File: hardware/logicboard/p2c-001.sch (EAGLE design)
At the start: 40 parts, among them IC1 74LS07N, K1 G5V1, T1 2SC1815

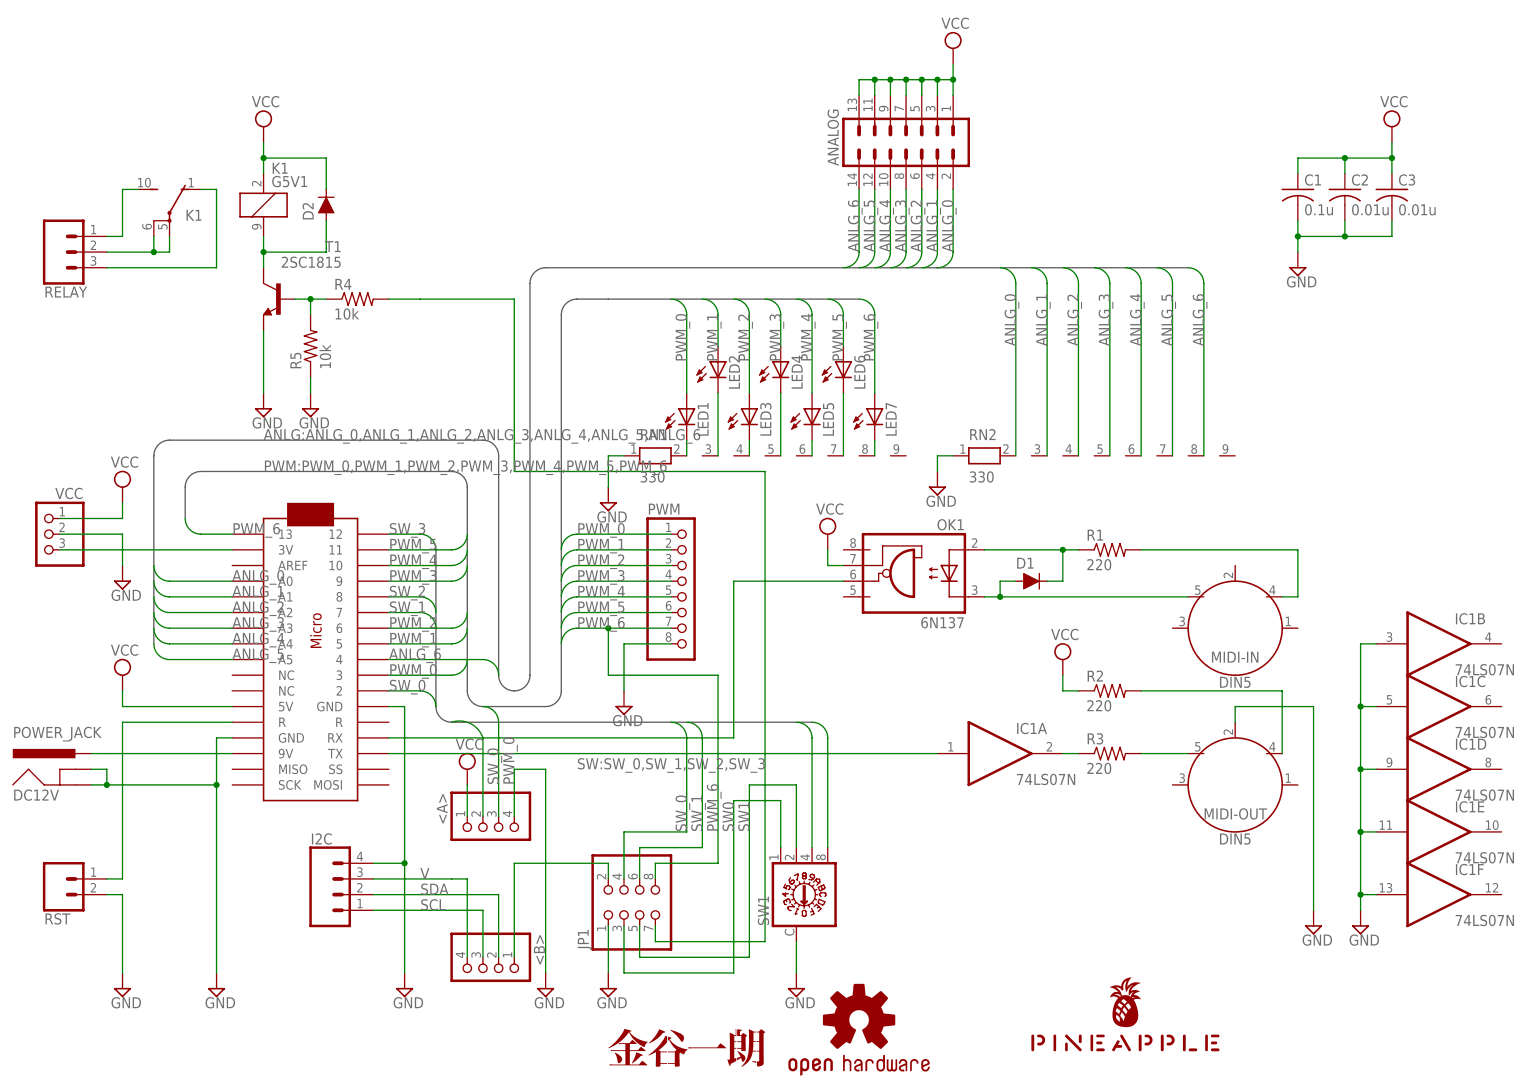
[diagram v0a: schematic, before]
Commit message: Alternative DC and MIDI connectors.
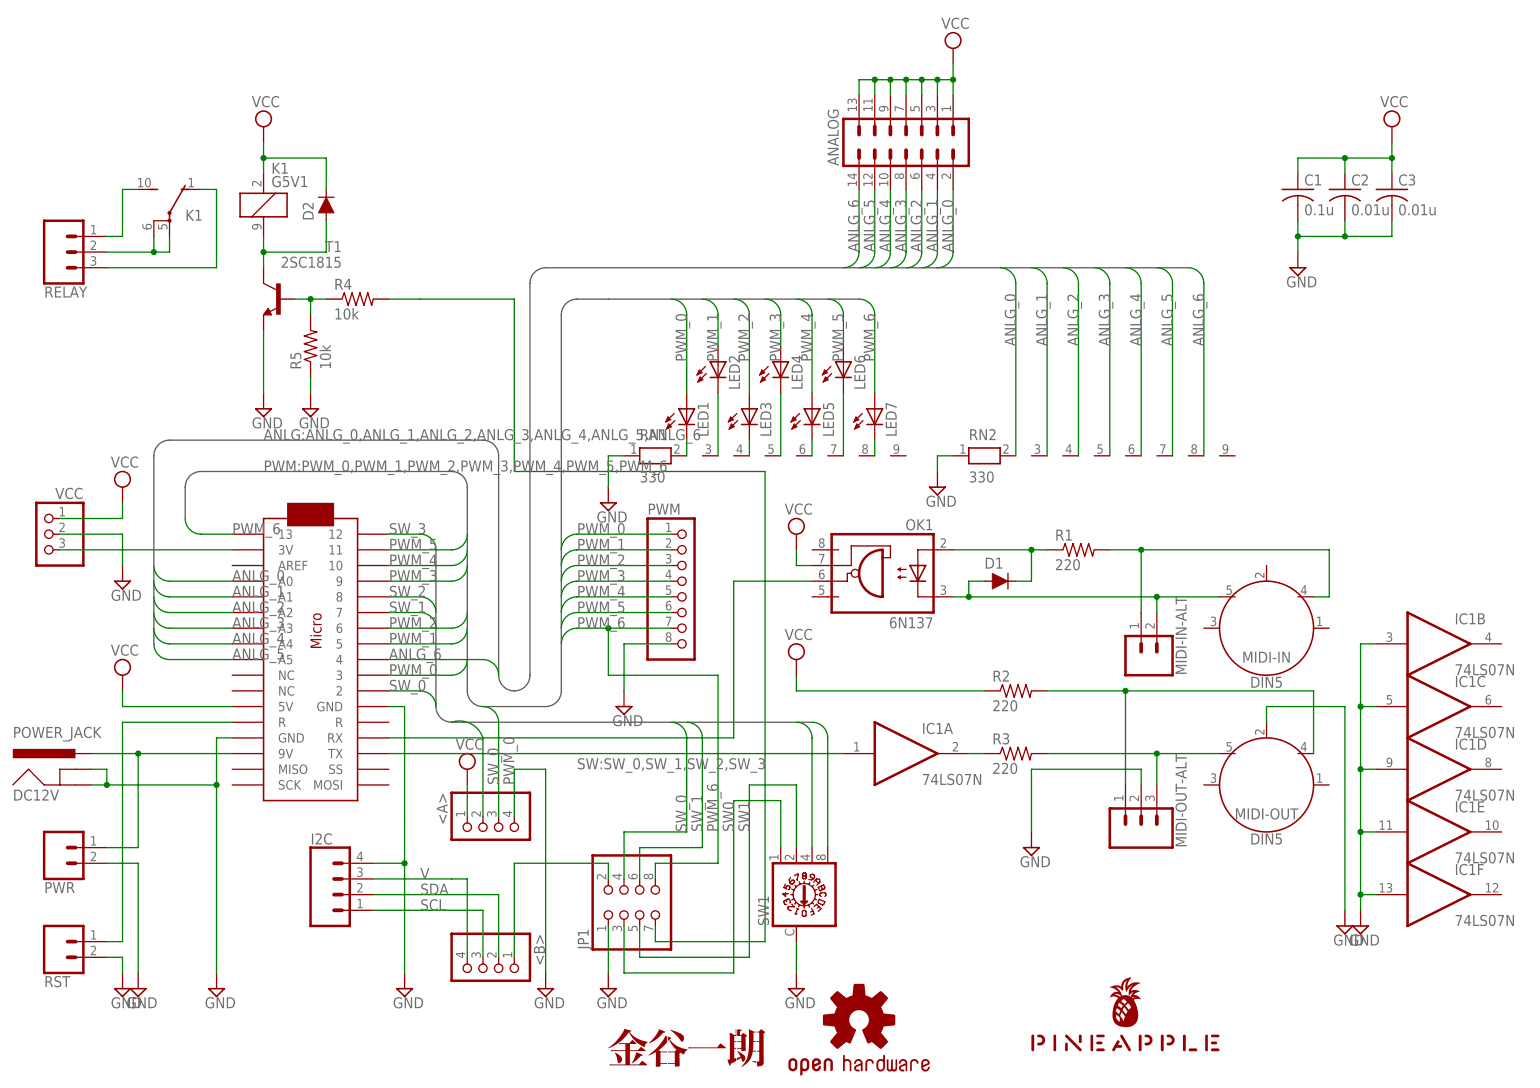
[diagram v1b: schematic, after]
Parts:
- added MIDI-IN-ALT: (no value), SparkFun-Connectors:CONN_02JST-PTH-2
- added MIDI-OUT-ALT: (no value), SparkFun-Connectors:CONN_03JST-PTH
- added PWR: (no value), SparkFun-Connectors:CONN_02
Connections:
- net GND: now also MIDI-OUT-ALT.2, PWR.2
- net MIDIIN+: now also MIDI-IN-ALT.1
- net MIDIIN-: now also MIDI-IN-ALT.2
- net MIDIOUT+: now also MIDI-OUT-ALT.1
- net MIDIOUT-: now also MIDI-OUT-ALT.3
- net VIN: now also PWR.1
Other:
- moved on the sheet: D1, IC1A, MIDI-IN, MIDI-OUT, OK1, R1, R2, R3, RST

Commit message: QR Code.
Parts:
- added U$4: CARD_QR, pineapple_card_qr:CARD_QR
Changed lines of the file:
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@@
 <part name="PWR" library="SparkFun-Connectors" library_urn="urn:adsk.eagle:library:513" deviceset="CONN_02" device="" package3d_urn="urn:adsk.eagle:package:38039/1"/>
 <part name="SUPPLY25" library="supply2" library_urn="urn:adsk.eagle:library:372" deviceset="GND" device=""/>
+<part name="U$4" library="pineapple_card_qr" deviceset="CARD_QR" device=""/>
 </parts>
 <sheets>
@@
 <instance part="PWR" gate="G$1" x="15.24" y="40.64" rot="MR180"/>
 <instance part="SUPPLY25" gate="GND" x="27.94" y="17.78"/>
+<instance part="U$4" gate="G$1" x="149.86" y="25.4"/>
 </instances>
 <busses>

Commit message: Now the name is printed by silk.
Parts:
- U$1: value PINEAPPLE450 -> PINEAPPLE450_SILK; device pineapple:PINEAPPLE450 -> pineapple:PINEAPPLE450_SILK
- U$3: value KANAYA -> KANAYA_SILK; device kanaya:KANAYA -> kanaya:KANAYA_SILK
- U$4: value CARD_QR -> PINEAPPLECARDQR_SILK; device pineapple_card_qr:CARD_QR -> pineapplecardqr:PINEAPPLECARDQR_SILK
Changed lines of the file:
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@@
 <parts>
 <part name="FRAME1" library="frames" library_urn="urn:adsk.eagle:library:229" deviceset="A4L-LOC" device=""/>
-<part name="U$1" library="pineapple" deviceset="PINEAPPLE450" device=""/>
+<part name="U$1" library="pineapple" deviceset="PINEAPPLE450_SILK" device=""/>
 <part name="U$2" library="adafruit" deviceset="ARDUINOMICRO" device=""/>
 <part name="SUPPLY1" library="supply2" library_urn="urn:adsk.eagle:library:372" deviceset="GND" device=""/>
@@
 <part name="SUPPLY19" library="supply2" library_urn="urn:adsk.eagle:library:372" deviceset="VCC" device=""/>
 <part name="SUPPLY20" library="supply2" library_urn="urn:adsk.eagle:library:372" deviceset="GND" device=""/>
-<part name="U$3" library="kanaya" deviceset="KANAYA" device=""/>
+<part name="U$3" library="kanaya" deviceset="KANAYA_SILK" device=""/>
 <part name="R4" library="resistor" library_urn="urn:adsk.eagle:library:348" deviceset="R-US_" device="0204/5" package3d_urn="urn:adsk.eagle:package:25955/1" value="10k"/>
 <part name="T1" library="transistor" library_urn="urn:adsk.eagle:library:402" deviceset="2SC1815" device="" package3d_urn="urn:adsk.eagle:package:29929/2"/>
@@
 <part name="PWR" library="SparkFun-Connectors" library_urn="urn:adsk.eagle:library:513" deviceset="CONN_02" device="" package3d_urn="urn:adsk.eagle:package:38039/1"/>
 <part name="SUPPLY25" library="supply2" library_urn="urn:adsk.eagle:library:372" deviceset="GND" device=""/>
-<part name="U$4" library="pineapple_card_qr" deviceset="CARD_QR" device=""/>
+<part name="U$4" library="pineapplecardqr" deviceset="PINEAPPLECARDQR_SILK" device=""/>
 </parts>
 <sheets>

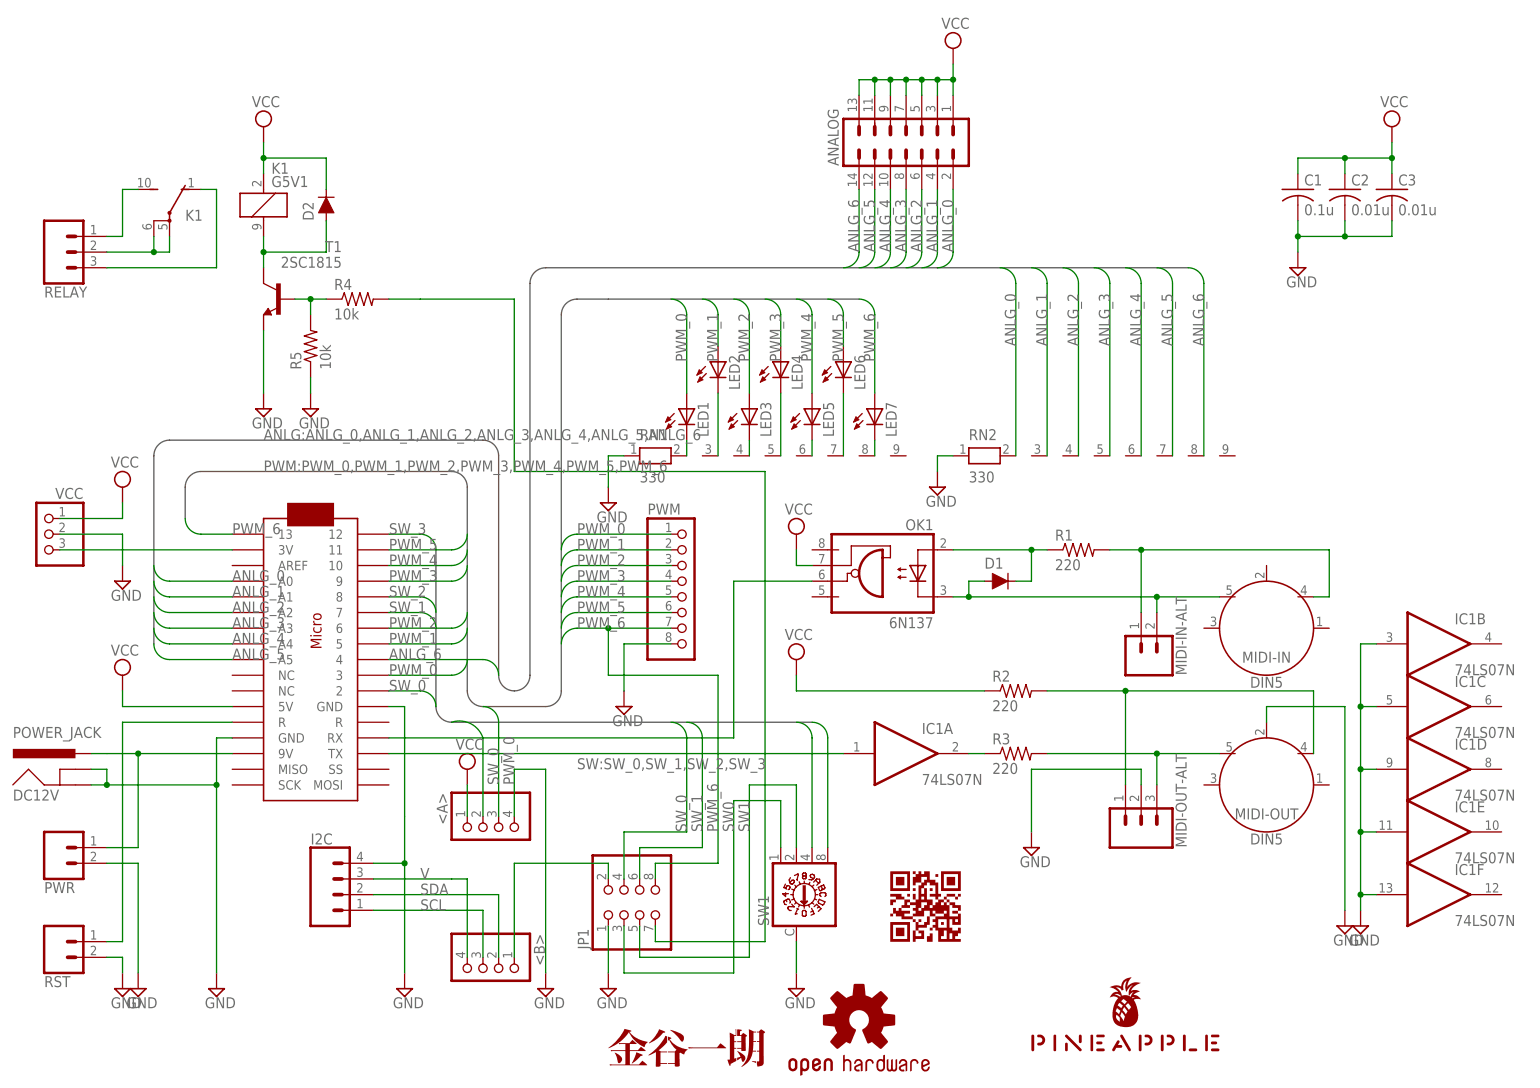
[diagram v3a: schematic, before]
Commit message: Changed OSHW logo from silk to copper.
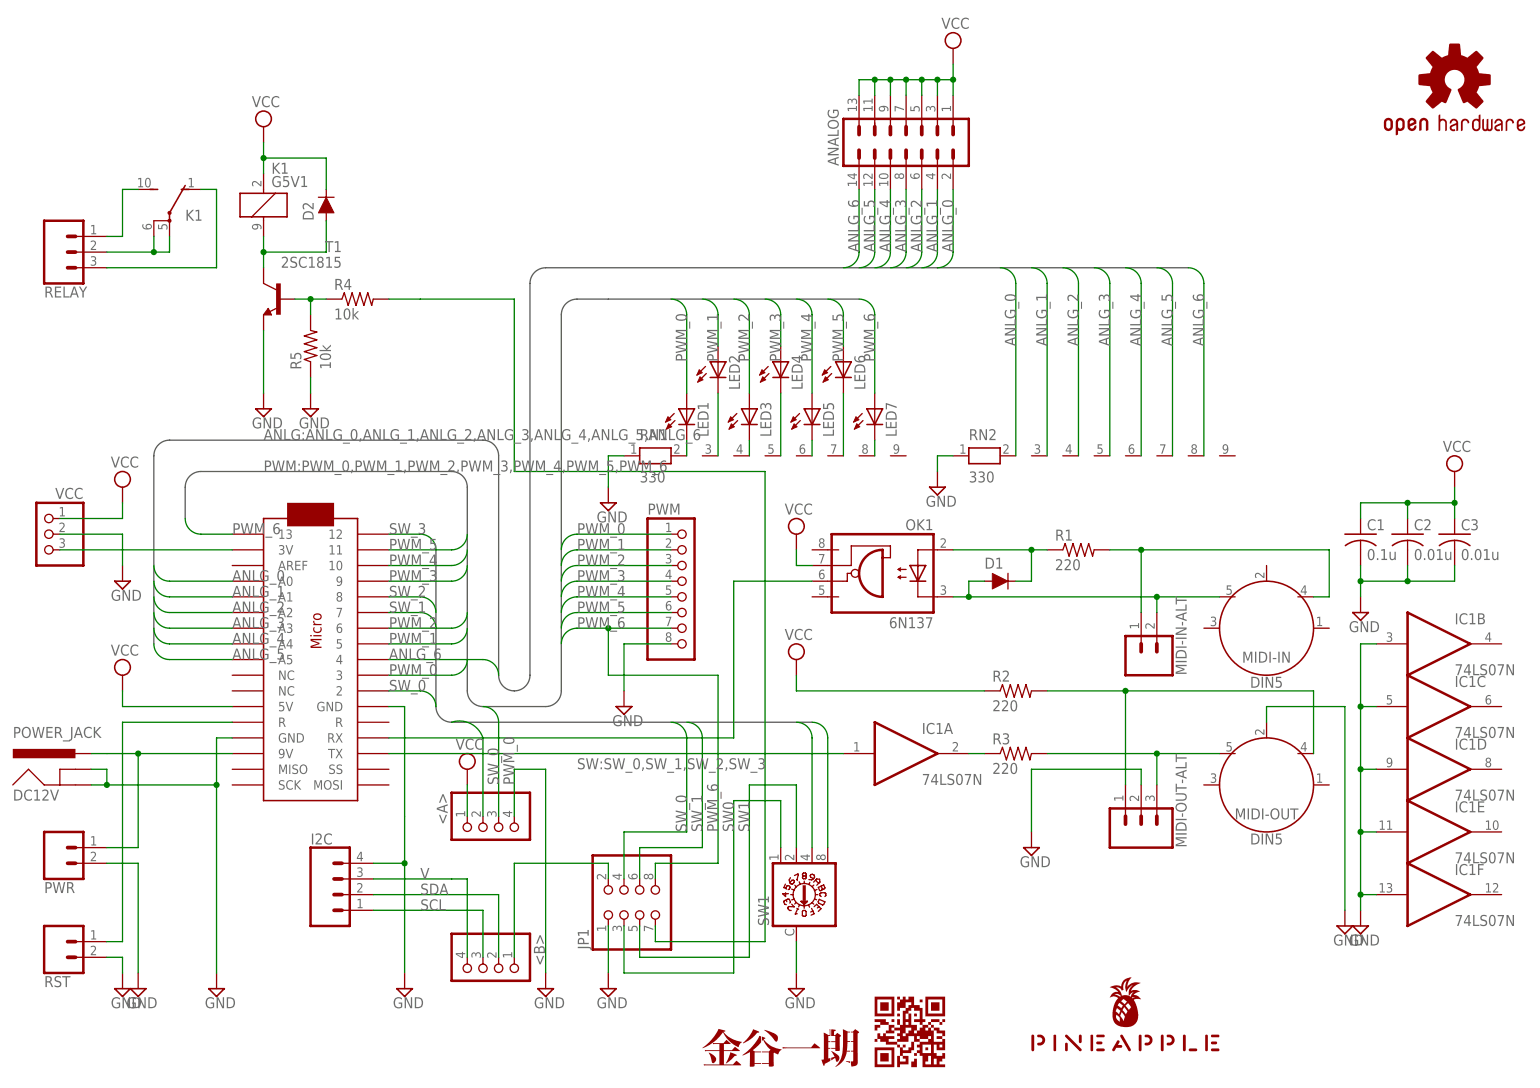
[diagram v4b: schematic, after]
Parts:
- LOGO1: value OSHW-LOGOS -> OSHW-LOGOS-COPPER; device SparkFun-Aesthetics:OSHW-LOGOS -> SparkFun-Aesthetics:OSHW-LOGOS-COPPER
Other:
- moved on the sheet: C1, C2, C3
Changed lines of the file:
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@@
 <part name="SUPPLY11" library="supply2" library_urn="urn:adsk.eagle:library:372" deviceset="GND" device=""/>
 <part name="SUPPLY12" library="supply2" library_urn="urn:adsk.eagle:library:372" deviceset="GND" device=""/>
-<part name="LOGO1" library="SparkFun-Aesthetics" deviceset="OSHW-LOGO" device="S"/>
+<part name="LOGO1" library="SparkFun-Aesthetics" deviceset="OSHW-LOGO" device="S-COPPER" value="OSHW-LOGOS-COPPER"/>
 <part name="RELAY" library="SparkFun-Connectors" library_urn="urn:adsk.eagle:library:513" deviceset="CONN_03" device="JST-PTH" package3d_urn="urn:adsk.eagle:package:38069/1"/>
 <part name="SUPPLY13" library="supply2" library_urn="urn:adsk.eagle:library:372" deviceset="GND" device=""/>
@@
 <instance part="RN2" gate="1" x="165.1" y="104.14"/>
 <instance part="SUPPLY9" gate="GND" x="157.48" y="99.06"/>
-<instance part="C1" gate="G$1" x="215.9" y="147.32"/>
-<instance part="C2" gate="G$1" x="223.52" y="147.32"/>
-<instance part="C3" gate="G$1" x="231.14" y="147.32"/>
-<instance part="SUPPLY10" gate="G$1" x="231.14" y="157.48"/>
-<instance part="SUPPLY11" gate="GND" x="215.9" y="134.62"/>
+<instance part="C1" gate="G$1" x="226.06" y="91.44"/>
+<instance part="C2" gate="G$1" x="233.68" y="91.44"/>
+<instance part="C3" gate="G$1" x="241.3" y="91.44"/>
+<instance part="SUPPLY10" gate="G$1" x="241.3" y="101.6"/>
+<instance part="SUPPLY11" gate="GND" x="226.06" y="78.74"/>
 <instance part="SUPPLY12" gate="GND" x="226.06" y="27.94"/>
-<instance part="LOGO1" gate="G$1" x="144.78" y="12.7"/>
+<instance part="LOGO1" gate="G$1" x="241.3" y="165.1"/>
 <instance part="RELAY" gate="J$1" x="15.24" y="137.16" rot="MR180"/>
 <instance part="SUPPLY13" gate="GND" x="25.4" y="17.78"/>
@@
 <instance part="SUPPLY19" gate="G$1" x="81.28" y="53.34"/>
 <instance part="SUPPLY20" gate="GND" x="93.98" y="17.78"/>
-<instance part="U$3" gate="G$1" x="116.84" y="5.08"/>
+<instance part="U$3" gate="G$1" x="132.08" y="5.08"/>
 <instance part="R4" gate="G$1" x="63.5" y="129.54"/>
 <instance part="T1" gate="G$1" x="50.8" y="129.54" rot="MR0"/>
@@
 <instance part="PWR" gate="G$1" x="15.24" y="40.64" rot="MR180"/>
 <instance part="SUPPLY25" gate="GND" x="27.94" y="17.78"/>
-<instance part="U$4" gate="G$1" x="149.86" y="25.4"/>
+<instance part="U$4" gate="G$1" x="147.32" y="5.08"/>
 </instances>
 <busses>
@@
 <pinref part="C1" gate="G$1" pin="2"/>
 <pinref part="SUPPLY11" gate="GND" pin="GND"/>
-<wire x1="215.9" y1="142.24" x2="215.9" y2="139.7" width="0.1524" layer="91"/>
+<wire x1="226.06" y1="86.36" x2="226.06" y2="83.82" width="0.1524" layer="91"/>
 <pinref part="C2" gate="G$1" pin="2"/>
-<wire x1="215.9" y1="139.7" x2="215.9" y2="137.16" width="0.1524" layer="91"/>
-<wire x1="223.52" y1="142.24" x2="223.52" y2="139.7" width="0.1524" layer="91"/>
-<wire x1="223.52" y1="139.7" x2="215.9" y2="139.7" width="0.1524" layer="91"/>
-<junction x="215.9" y="139.7"/>
+<wire x1="226.06" y1="83.82" x2="226.06" y2="81.28" width="0.1524" layer="91"/>
+<wire x1="233.68" y1="86.36" x2="233.68" y2="83.82" width="0.1524" layer="91"/>
+<wire x1="233.68" y1="83.82" x2="226.06" y2="83.82" width="0.1524" layer="91"/>
+<junction x="226.06" y="83.82"/>
 <pinref part="C3" gate="G$1" pin="2"/>
-<wire x1="231.14" y1="142.24" x2="231.14" y2="139.7" width="0.1524" layer="91"/>
-<wire x1="231.14" y1="139.7" x2="223.52" y2="139.7" width="0.1524" layer="91"/>
-<junction x="223.52" y="139.7"/>
+<wire x1="241.3" y1="86.36" x2="241.3" y2="83.82" width="0.1524" layer="91"/>
+<wire x1="241.3" y1="83.82" x2="233.68" y2="83.82" width="0.1524" layer="91"/>
+<junction x="233.68" y="83.82"/>
 </segment>
 <segment>
@@
 <pinref part="SUPPLY10" gate="G$1" pin="VCC"/>
 <pinref part="C3" gate="G$1" pin="1"/>
-<wire x1="231.14" y1="154.94" x2="231.14" y2="152.4" width="0.1524" layer="91"/>
-<wire x1="231.14" y1="152.4" x2="231.14" y2="149.86" width="0.1524" layer="91"/>
-<wire x1="231.14" y1="152.4" x2="223.52" y2="152.4" width="0.1524" layer="91"/>
-<junction x="231.14" y="152.4"/>
+<wire x1="241.3" y1="99.06" x2="241.3" y2="96.52" width="0.1524" layer="91"/>
+<wire x1="241.3" y1="96.52" x2="241.3" y2="93.98" width="0.1524" layer="91"/>
+<wire x1="241.3" y1="96.52" x2="233.68" y2="96.52" width="0.1524" layer="91"/>
+<junction x="241.3" y="96.52"/>
 <pinref part="C2" gate="G$1" pin="1"/>
-<wire x1="223.52" y1="152.4" x2="223.52" y2="149.86" width="0.1524" layer="91"/>
-<wire x1="223.52" y1="152.4" x2="215.9" y2="152.4" width="0.1524" layer="91"/>
-<junction x="223.52" y="152.4"/>
+<wire x1="233.68" y1="96.52" x2="233.68" y2="93.98" width="0.1524" layer="91"/>
+<wire x1="233.68" y1="96.52" x2="226.06" y2="96.52" width="0.1524" layer="91"/>
+<junction x="233.68" y="96.52"/>
 <pinref part="C1" gate="G$1" pin="1"/>
-<wire x1="215.9" y1="152.4" x2="215.9" y2="149.86" width="0.1524" layer="91"/>
-</segment>
-<segment>
+<wire x1="226.06" y1="96.52" x2="226.06" y2="93.98" width="0.1524" layer="91"/>
+</segment>
+<segment>
